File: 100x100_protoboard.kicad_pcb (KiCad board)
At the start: 2 copper layers, 97.8 x 96.5 mm, 422 parts, among them CON1 BARREL_JACK, CON2 USB_FEMALE_WITH_ID, CON3 USB_FEMALE_WITH_ID, J1 INTERCONNECT_1X03, J10 INTERCONNECT_1X03, J11 INTERCONNECT_1X03, J12 INTERCONNECT_1X03, J13 INTERCONNECT_1X03, J14 INTERCONNECT_1X03, J15 INTERCONNECT_1X03, J16 INTERCONNECT_1X03, J17 INTERCONNECT_1X03, J18 INTERCONNECT_1X03, J19 INTERCONNECT_1X03, J2 INTERCONNECT_1X03, J20 INTERCONNECT_1X03, J21 INTERCONNECT_1X03, J22 INTERCONNECT_1X03, J23 INTERCONNECT_1X03, J24 INTERCONNECT_1X03, J25 INTERCONNECT_1X03, J26 INTERCONNECT_1X03, J27 INTERCONNECT_1X03, J28 INTERCONNECT_1X03, J29 INTERCONNECT_1X03, J3 INTERCONNECT_1X03, J30 INTERCONNECT_1X03, J31 INTERCONNECT_1X03, J32 INTERCONNECT_1X03, J33 INTERCONNECT_1X03, J34 INTERCONNECT_1X03, J35 INTERCONNECT_1X03, J36 INTERCONNECT_1X03, J37 INTERCONNECT_1X03, J38 INTERCONNECT_1X03, J39 INTERCONNECT_1X03, J4 INTERCONNECT_1X03, J40 INTERCONNECT_1X03, J41 INTERCONNECT_1X03, J42 INTERCONNECT_1X03, J43 INTERCONNECT_1X03, J44 INTERCONNECT_1X03, J45 INTERCONNECT_1X03, J46 INTERCONNECT_1X03, J47 INTERCONNECT_1X03, J48 INTERCONNECT_1X03, J49 INTERCONNECT_1X03, J5 INTERCONNECT_1X03, J50 INTERCONNECT_1X03, J51 INTERCONNECT_1X03, J52 INTERCONNECT_1X03, J53 INTERCONNECT_1X03, J54 INTERCONNECT_1X03, J55 INTERCONNECT_1X03, J56 INTERCONNECT_1X03, J57 INTERCONNECT_1X03, J58 INTERCONNECT_1X03, J59 INTERCONNECT_1X03, J6 INTERCONNECT_1X03, J60 INTERCONNECT_1X03, J61 INTERCONNECT_1X03, J62 INTERCONNECT_1X03, J63 INTERCONNECT_1X03, J64 INTERCONNECT_1X03, J65 INTERCONNECT_1X02, J7 INTERCONNECT_1X03, J8 INTERCONNECT_1X03, J9 INTERCONNECT_1X03, P1 CONN_5, P1 CONN_6X2, P2 CONN_6X2, U1 LM7805CT

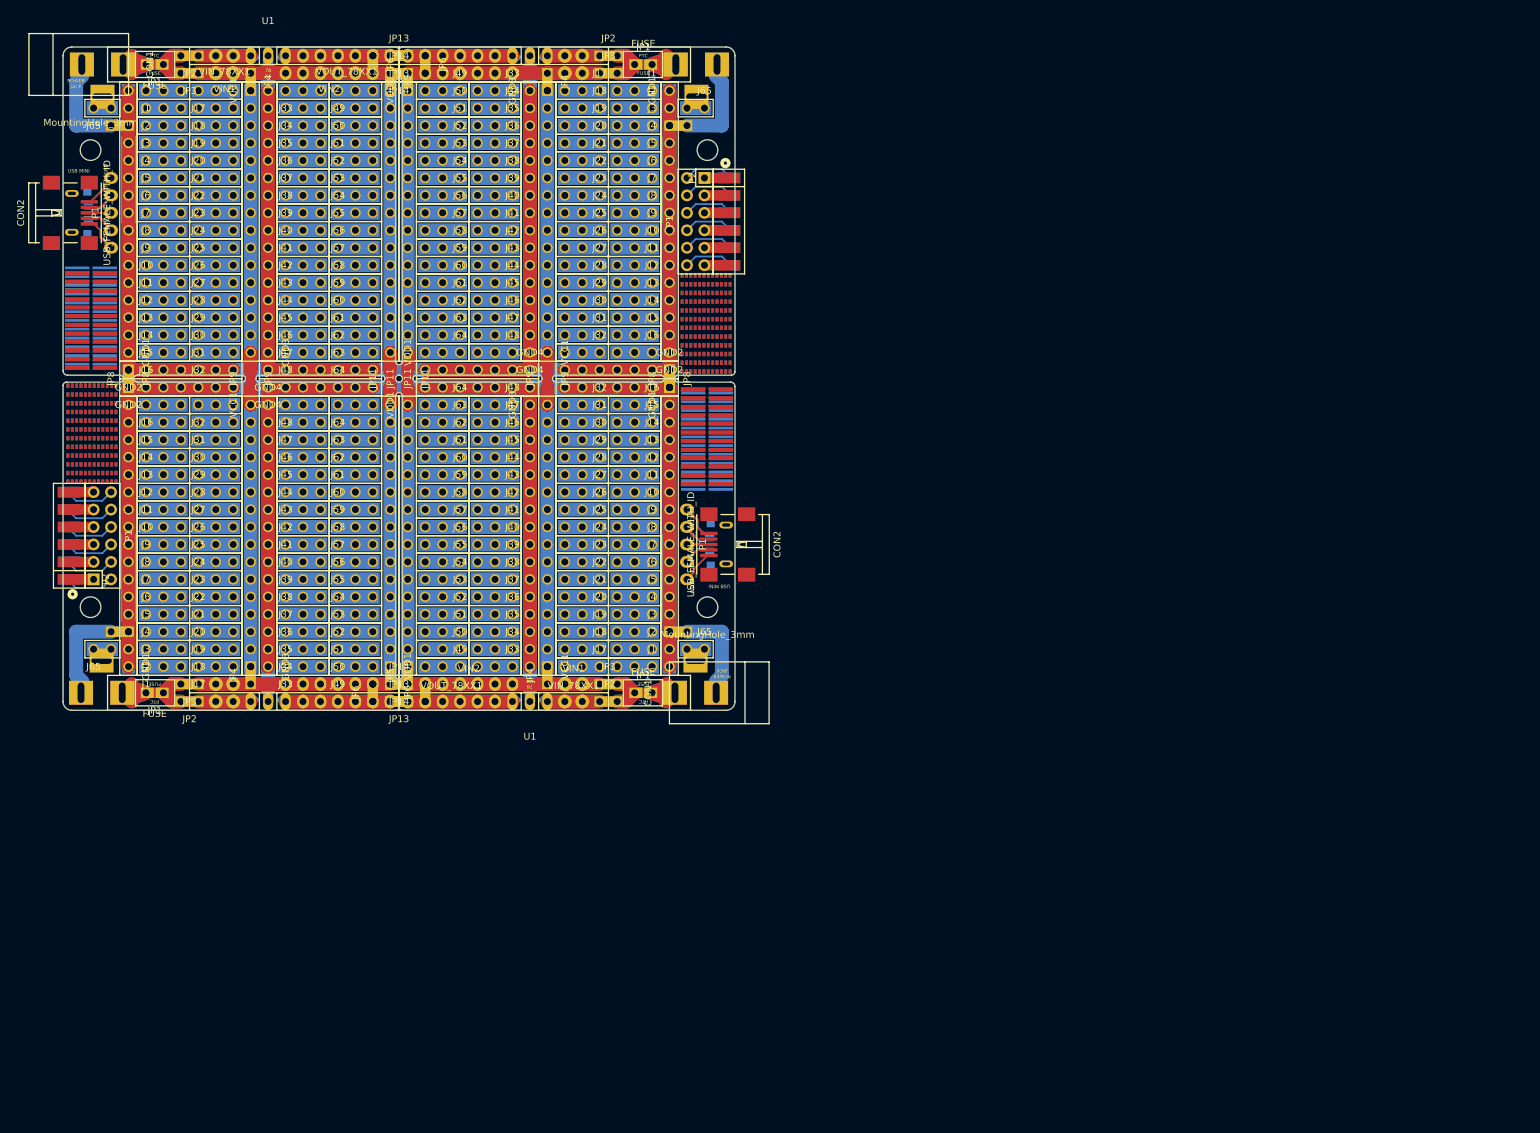
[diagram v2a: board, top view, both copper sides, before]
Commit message: increased pad size for SMD grid on bottom-left quarter
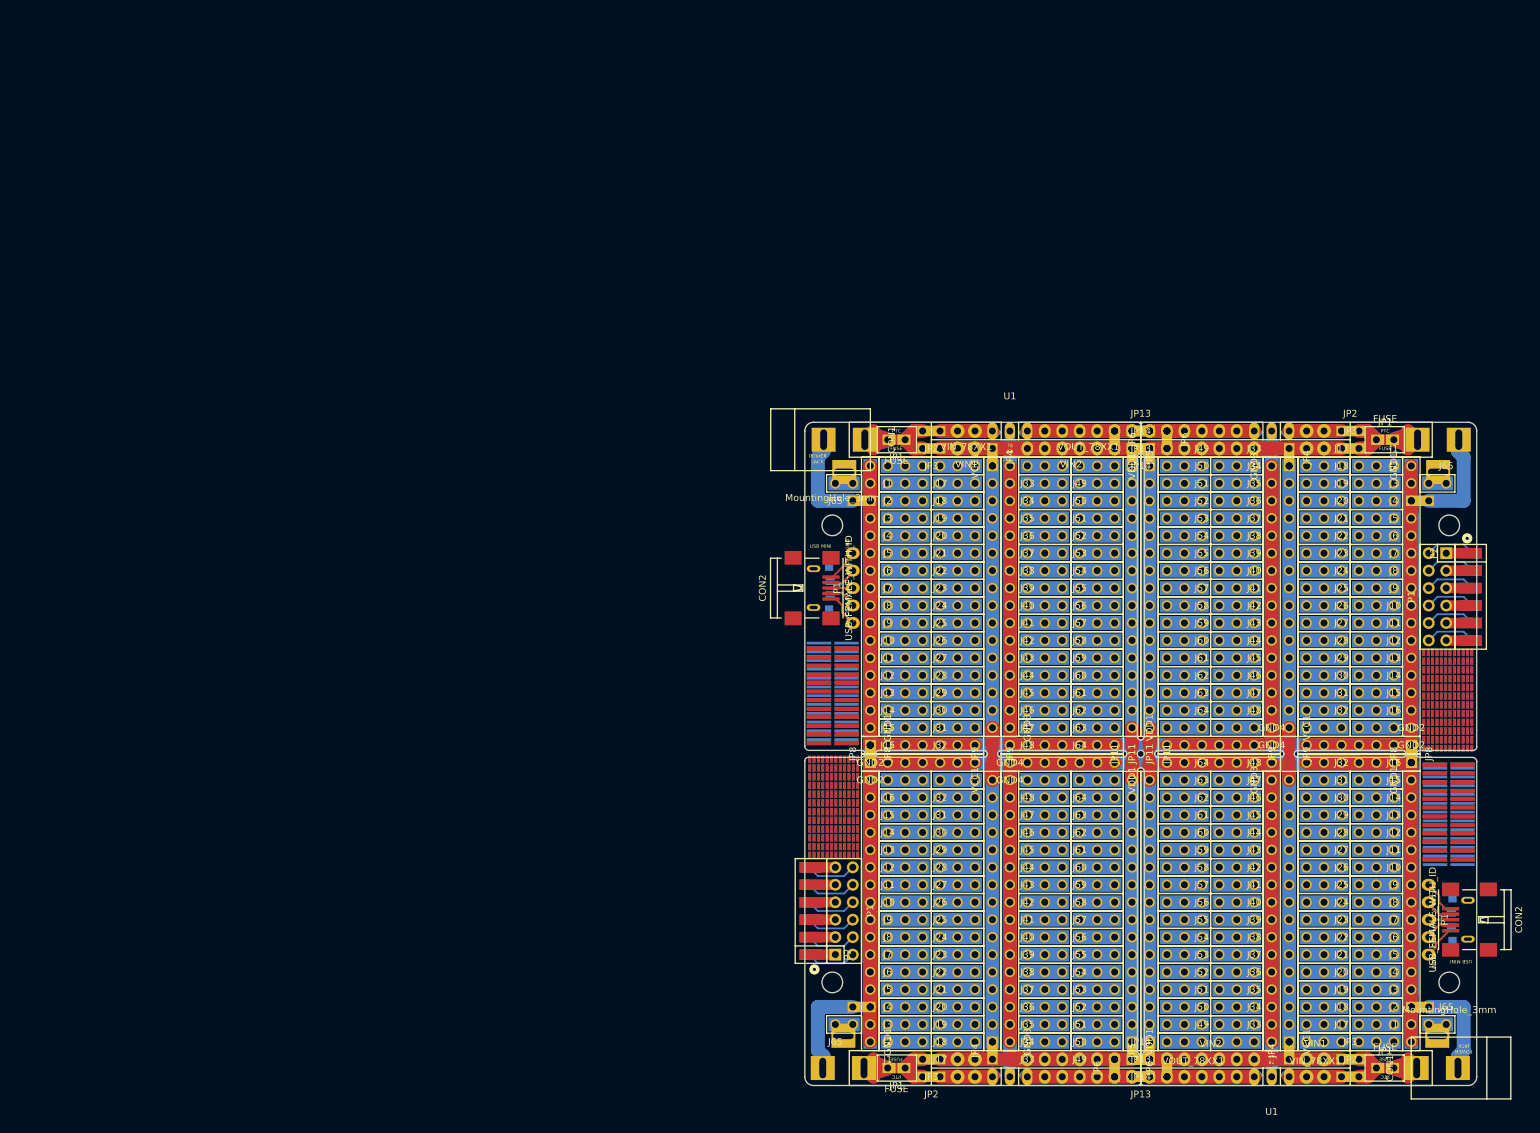
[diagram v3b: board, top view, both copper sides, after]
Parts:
- removed the C1 at (50.8, 117.1)
- removed the C1 at (91.4, 117.1)
- removed the C1 at (50.8, 25.1)
- removed the C1 at (91.4, 25.1)
- removed the C2 at (53.3, 117.1)
- removed the C2 at (88.9, 117.1)
- removed the C2 at (53.3, 25.1)
- removed the C2 at (88.9, 25.1)
- removed the CON1 at (24.6, 116.8)
- removed the CON1 at (117.5, 116.8)
- removed the CON1 at (24.8, 25.4)
- removed the CON1 at (117.6, 25.4)
- removed the CON2 at (116.2, 95.2)
- removed the CON2 at (26.0, 47.0)
- removed the CON3 at (116.3, 95.2)
- removed the CON3 at (25.9, 47.0)
- removed the F1 at (35.6, 116.8)
- removed the F1 at (106.7, 116.8)
- removed the F1 at (35.6, 25.4)
- removed the F1 at (106.7, 25.4)
- removed the F2 at (35.6, 116.8)
- removed the F2 at (106.7, 116.8)
- removed the F2 at (35.6, 25.4)
- removed the F2 at (106.7, 25.4)
- removed the GND1 at (31.8, 113.0)
- removed the GND1 at (110.5, 74.9)
- removed the GND1 at (31.8, 67.3)
- removed the GND1 at (110.5, 29.2)
- removed the GND2 at (31.8, 72.4)
- removed the GND2 at (110.5, 72.4)
- removed the GND2 at (31.8, 69.8)
- removed the GND2 at (110.5, 69.8)
- removed the GND3 at (52.1, 113.0)
- removed the GND3 at (90.2, 74.9)
- removed the GND3 at (52.1, 67.3)
- removed the GND3 at (90.2, 29.2)
- removed the GND4 at (52.1, 72.4)
- removed the GND4 at (90.2, 72.4)
- removed the GND4 at (52.1, 69.8)
- removed the GND4 at (90.2, 69.8)
- removed the J1 at (34.3, 113.0)
- removed the J1 at (108.0, 113.0)
- removed the J1 at (34.3, 29.2)
- removed the J1 at (108.0, 29.2)
- removed the J10 at (34.3, 90.2)
- removed the J10 at (108.0, 90.2)
- removed the J10 at (34.3, 52.1)
- removed the J10 at (108.0, 52.1)
- removed the J11 at (34.3, 87.6)
- removed the J11 at (108.0, 87.6)
- removed the J11 at (34.3, 54.6)
- removed the J11 at (108.0, 54.6)
- removed the J12 at (34.3, 85.1)
- removed the J12 at (108.0, 85.1)
- removed the J12 at (34.3, 57.1)
- removed the J12 at (108.0, 57.1)
- removed the J13 at (34.3, 82.5)
- removed the J13 at (108.0, 82.5)
- removed the J13 at (34.3, 59.7)
- removed the J13 at (108.0, 59.7)
- removed the J14 at (34.3, 80.0)
- removed the J14 at (108.0, 80.0)
- removed the J14 at (34.3, 62.2)
- removed the J14 at (108.0, 62.2)
- removed the J15 at (34.3, 77.5)
- removed the J15 at (108.0, 77.5)
- removed the J15 at (34.3, 64.8)
- removed the J15 at (108.0, 64.8)
- removed the J16 at (34.3, 74.9)
- removed the J16 at (108.0, 74.9)
- removed the J16 at (34.3, 67.3)
- removed the J16 at (108.0, 67.3)
- removed the J17 at (41.9, 113.0)
- removed the J17 at (100.3, 113.0)
- removed the J17 at (41.9, 29.2)
- removed the J17 at (100.3, 29.2)
- removed the J18 at (41.9, 110.5)
- removed the J18 at (100.3, 110.5)
- removed the J18 at (41.9, 31.8)
- removed the J18 at (100.3, 31.8)
- removed the J19 at (41.9, 108.0)
- removed the J19 at (100.3, 108.0)
- removed the J19 at (41.9, 34.3)
- removed the J19 at (100.3, 34.3)
- removed the J2 at (34.3, 110.5)
- removed the J2 at (108.0, 110.5)
- removed the J2 at (34.3, 31.8)
- removed the J2 at (108.0, 31.8)
- removed the J20 at (41.9, 105.4)
- removed the J20 at (100.3, 105.4)
- removed the J20 at (41.9, 36.8)
- removed the J20 at (100.3, 36.8)
- removed the J21 at (41.9, 102.9)
- removed the J21 at (100.3, 102.9)
- removed the J21 at (41.9, 39.4)
- removed the J21 at (100.3, 39.4)
- removed the J22 at (41.9, 100.3)
- removed the J22 at (100.3, 100.3)
- removed the J22 at (41.9, 41.9)
- removed the J22 at (100.3, 41.9)
- removed the J23 at (41.9, 97.8)
- removed the J23 at (100.3, 97.8)
- removed the J23 at (41.9, 44.5)
- removed the J23 at (100.3, 44.5)
- removed the J24 at (41.9, 95.2)
- removed the J24 at (100.3, 95.2)
- removed the J24 at (41.9, 47.0)
- removed the J24 at (100.3, 47.0)
- removed the J25 at (41.9, 92.7)
- removed the J25 at (100.3, 92.7)
- removed the J25 at (41.9, 49.5)
- removed the J25 at (100.3, 49.5)
- removed the J26 at (41.9, 90.2)
- removed the J26 at (100.3, 90.2)
- removed the J26 at (41.9, 52.1)
- removed the J26 at (100.3, 52.1)
- removed the J27 at (41.9, 87.6)
- removed the J27 at (100.3, 87.6)
- removed the J27 at (41.9, 54.6)
- removed the J27 at (100.3, 54.6)
- removed the J28 at (41.9, 85.1)
- removed the J28 at (100.3, 85.1)
- removed the J28 at (41.9, 57.1)
- removed the J28 at (100.3, 57.1)
- removed the J29 at (41.9, 82.5)
- removed the J29 at (100.3, 82.5)
- removed the J29 at (41.9, 59.7)
- removed the J29 at (100.3, 59.7)
- removed the J3 at (34.3, 108.0)
- removed the J3 at (108.0, 108.0)
- removed the J3 at (34.3, 34.3)
- removed the J3 at (108.0, 34.3)
- removed the J30 at (41.9, 80.0)
- removed the J30 at (100.3, 80.0)
- removed the J30 at (41.9, 62.2)
- removed the J30 at (100.3, 62.2)
- removed the J31 at (41.9, 77.5)
- removed the J31 at (100.3, 77.5)
- removed the J31 at (41.9, 64.8)
- removed the J31 at (100.3, 64.8)
- removed the J32 at (41.9, 74.9)
- removed the J32 at (100.3, 74.9)
- removed the J32 at (41.9, 67.3)
- removed the J32 at (100.3, 67.3)
- removed the J33 at (54.6, 113.0)
- removed the J33 at (87.6, 113.0)
- removed the J33 at (54.6, 29.2)
- removed the J33 at (87.6, 29.2)
- removed the J34 at (54.6, 110.5)
- removed the J34 at (87.6, 110.5)
- removed the J34 at (54.6, 31.8)
- removed the J34 at (87.6, 31.8)
- removed the J35 at (54.6, 108.0)
- removed the J35 at (87.6, 108.0)
- removed the J35 at (54.6, 34.3)
- removed the J35 at (87.6, 34.3)
- removed the J36 at (54.6, 105.4)
- removed the J36 at (87.6, 105.4)
- removed the J36 at (54.6, 36.8)
- removed the J36 at (87.6, 36.8)
- removed the J37 at (54.6, 102.9)
- removed the J37 at (87.6, 102.9)
- removed the J37 at (54.6, 39.4)
- removed the J37 at (87.6, 39.4)
- removed the J38 at (54.6, 100.3)
- removed the J38 at (87.6, 100.3)
- removed the J38 at (54.6, 41.9)
- removed the J38 at (87.6, 41.9)
- removed the J39 at (54.6, 97.8)
- removed the J39 at (87.6, 97.8)
- removed the J39 at (54.6, 44.5)
- removed the J39 at (87.6, 44.5)
- removed the J4 at (34.3, 105.4)
- removed the J4 at (108.0, 105.4)
- removed the J4 at (34.3, 36.8)
- removed the J4 at (108.0, 36.8)
- removed the J40 at (54.6, 95.2)
- removed the J40 at (87.6, 95.2)
- removed the J40 at (54.6, 47.0)
- removed the J40 at (87.6, 47.0)
- removed the J41 at (54.6, 92.7)
- removed the J41 at (87.6, 92.7)
- removed the J41 at (54.6, 49.5)
- removed the J41 at (87.6, 49.5)
- removed the J42 at (54.6, 90.2)
- removed the J42 at (87.6, 90.2)
- removed the J42 at (54.6, 52.1)
- removed the J42 at (87.6, 52.1)
- removed the J43 at (54.6, 87.6)
- removed the J43 at (87.6, 87.6)
- removed the J43 at (54.6, 54.6)
- removed the J43 at (87.6, 54.6)
- removed the J44 at (54.6, 85.1)
- removed the J44 at (87.6, 85.1)
- removed the J44 at (54.6, 57.1)
- removed the J44 at (87.6, 57.1)
- removed the J45 at (54.6, 82.5)
- removed the J45 at (87.6, 82.5)
- removed the J45 at (54.6, 59.7)
- removed the J45 at (87.6, 59.7)
- removed the J46 at (54.6, 80.0)
- removed the J46 at (87.6, 80.0)
- removed the J46 at (54.6, 62.2)
- removed the J46 at (87.6, 62.2)
- removed the J47 at (54.6, 77.5)
- removed the J47 at (87.6, 77.5)
- removed the J47 at (54.6, 64.8)
- removed the J47 at (87.6, 64.8)
- removed the J48 at (54.6, 74.9)
- removed the J48 at (87.6, 74.9)
- removed the J48 at (54.6, 67.3)
- removed the J48 at (87.6, 67.3)
- removed the J49 at (62.2, 113.0)
- removed the J49 at (80.0, 113.0)
- removed the J49 at (62.2, 29.2)
- removed the J49 at (80.0, 29.2)
- removed the J5 at (34.3, 102.9)
- removed the J5 at (108.0, 102.9)
- removed the J5 at (34.3, 39.4)
- removed the J5 at (108.0, 39.4)
- removed the J50 at (62.2, 110.5)
- removed the J50 at (80.0, 110.5)
- removed the J50 at (62.2, 31.8)
- removed the J50 at (80.0, 31.8)
- removed the J51 at (62.2, 108.0)
- removed the J51 at (80.0, 108.0)
- removed the J51 at (62.2, 34.3)
- removed the J51 at (80.0, 34.3)
- removed the J52 at (62.2, 105.4)
- removed the J52 at (80.0, 105.4)
- removed the J52 at (62.2, 36.8)
- removed the J52 at (80.0, 36.8)
- removed the J53 at (62.2, 102.9)
- removed the J53 at (80.0, 102.9)
- removed the J53 at (62.2, 39.4)
- removed the J53 at (80.0, 39.4)
- removed the J54 at (62.2, 100.3)
- removed the J54 at (80.0, 100.3)
- removed the J54 at (62.2, 41.9)
- removed the J54 at (80.0, 41.9)
- removed the J55 at (62.2, 97.8)
- removed the J55 at (80.0, 97.8)
- removed the J55 at (62.2, 44.5)
- removed the J55 at (80.0, 44.5)
- removed the J56 at (62.2, 95.2)
- removed the J56 at (80.0, 95.2)
- removed the J56 at (62.2, 47.0)
- removed the J56 at (80.0, 47.0)
- removed the J57 at (62.2, 92.7)
- removed the J57 at (80.0, 92.7)
- removed the J57 at (62.2, 49.5)
- removed the J57 at (80.0, 49.5)
- removed the J58 at (62.2, 90.2)
- removed the J58 at (80.0, 90.2)
- removed the J58 at (62.2, 52.1)
- removed the J58 at (80.0, 52.1)
- removed the J59 at (62.2, 87.6)
- removed the J59 at (80.0, 87.6)
- removed the J59 at (62.2, 54.6)
- removed the J59 at (80.0, 54.6)
- removed the J6 at (34.3, 100.3)
- removed the J6 at (108.0, 100.3)
- removed the J6 at (34.3, 41.9)
- removed the J6 at (108.0, 41.9)
- removed the J60 at (62.2, 85.1)
- removed the J60 at (80.0, 85.1)
- removed the J60 at (62.2, 57.1)
- removed the J60 at (80.0, 57.1)
- removed the J61 at (62.2, 82.5)
- removed the J61 at (80.0, 82.5)
- removed the J61 at (62.2, 59.7)
- removed the J61 at (80.0, 59.7)
- removed the J62 at (62.2, 80.0)
- removed the J62 at (80.0, 80.0)
- removed the J62 at (62.2, 62.2)
- removed the J62 at (80.0, 62.2)
- removed the J63 at (62.2, 77.5)
- removed the J63 at (80.0, 77.5)
- removed the J63 at (62.2, 64.8)
- removed the J63 at (80.0, 64.8)
- removed the J64 at (62.2, 74.9)
- removed the J64 at (80.0, 74.9)
- removed the J64 at (62.2, 67.3)
- removed the J64 at (80.0, 67.3)
- removed the J65 at (26.7, 110.5)
- removed the J65 at (115.6, 110.5)
- removed the J65 at (26.7, 31.8)
- removed the J65 at (115.6, 31.8)
- removed the J7 at (34.3, 97.8)
- removed the J7 at (108.0, 97.8)
- removed the J7 at (34.3, 44.5)
- removed the J7 at (108.0, 44.5)
- removed the J8 at (34.3, 95.2)
- removed the J8 at (108.0, 95.2)
- removed the J8 at (34.3, 47.0)
- removed the J8 at (108.0, 47.0)
- removed the J9 at (34.3, 92.7)
- removed the J9 at (108.0, 92.7)
- removed the J9 at (34.3, 49.5)
- removed the J9 at (108.0, 49.5)
- removed the JP1 at (35.6, 116.8)
- removed the JP1 at (106.7, 116.8)
- removed the JP1 at (35.6, 25.4)
- removed the JP1 at (106.7, 25.4)
- removed the JP10 at (69.8, 71.1) (x2)
- removed the JP10 at (72.4, 71.1) (x2)
- removed the JP11 at (69.8, 71.1) (x2)
- removed the JP11 at (72.4, 71.1) (x2)
- removed the JP12 at (71.1, 72.4) (x2)
- removed the JP12 at (71.1, 69.8) (x2)
- removed the JP13 at (71.1, 118.1) (x2)
- removed the JP13 at (71.1, 24.1) (x2)
- removed the JP14 at (71.1, 115.6) (x2)
- removed the JP14 at (71.1, 26.7) (x2)
- removed the JP15 at (49.5, 71.1) (x2)
- removed the JP15 at (92.7, 71.1) (x2)
- removed the JP2 at (40.6, 118.1)
- removed the JP2 at (101.6, 118.1)
- removed the JP2 at (40.6, 24.1)
- removed the JP2 at (101.6, 24.1)
- removed the JP3 at (40.6, 115.6)
- removed the JP3 at (101.6, 115.6)
- removed the JP3 at (40.6, 26.7)
- removed the JP3 at (101.6, 26.7)
- removed the JP4 at (49.5, 114.3)
- removed the JP4 at (92.7, 114.3)
- removed the JP4 at (49.5, 27.9)
- removed the JP4 at (92.7, 27.9)
- removed the JP5 at (69.8, 114.3)
- removed the JP5 at (72.4, 114.3)
- removed the JP5 at (69.8, 27.9)
- removed the JP5 at (72.4, 27.9)
- removed the JP6 at (67.3, 116.8)
- removed the JP6 at (74.9, 116.8)
- removed the JP6 at (67.3, 25.4)
- removed the JP6 at (74.9, 25.4)
- removed the JP7 at (30.5, 108.0)
- removed the JP7 at (111.8, 108.0)
- removed the JP7 at (30.5, 34.3)
- removed the JP7 at (111.8, 34.3)
- removed the JP8 at (31.8, 71.1) (x2)
- removed the JP8 at (110.5, 71.1) (x2)
- removed the JP9 at (49.5, 71.1) (x2)
- removed the JP9 at (92.7, 71.1) (x2)
- removed the MountingHole_3mm at (26.2, 104.4)
- removed the MountingHole_3mm at (116.0, 104.4)
- removed the MountingHole_3mm at (26.2, 37.9)
- removed the MountingHole_3mm at (116.0, 37.9)
- removed the P1 at (27.9, 94.0)
- removed the P1 at (113.0, 95.2)
- removed the P1 at (29.2, 47.0)
- removed the P1 at (114.3, 48.3)
- removed the P2 at (23.1, 100.3)
- removed the P2 at (119.1, 41.9)
- removed the Ref** at (25.8, 84.2) (x2)
- removed the Ref** at (116.0, 74.8)
- removed the Ref** at (116.0, 79.9)
- removed the Ref** at (116.0, 85.0)
- removed the Ref** at (26.3, 57.2)
- removed the Ref** at (26.3, 62.3)
- removed the Ref** at (26.3, 67.4)
- removed the Ref** at (26.3, 67.6)
- removed the Ref** at (26.3, 62.7)
- removed the Ref** at (26.3, 57.7)
- removed the Ref** at (116.5, 68.2) (x2)
- removed the Ref** at (25.8, 79.1) (x2)
- removed the Ref** at (116.5, 63.1) (x2)
- removed the Ref** at (116.5, 58.0) (x2)
- removed the Ref** at (25.8, 74.1) (x2)
- removed the Ref** at (115.9, 84.5)
- removed the Ref** at (115.9, 79.6)
- removed the Ref** at (115.9, 74.6)
- removed the U1 at (52.1, 118.1)
- removed the U1 at (90.2, 118.1)
- removed the U1 at (52.1, 24.1)
- removed the U1 at (90.2, 24.1)
- removed the VCC1 at (49.5, 74.9)
- removed the VCC1 at (92.7, 113.0)
- removed the VCC1 at (49.5, 29.2)
- removed the VCC1 at (92.7, 67.3)
- removed the VDD1 at (69.8, 113.0)
- removed the VDD1 at (72.4, 74.9)
- removed the VDD1 at (69.8, 67.3)
- removed the VDD1 at (72.4, 29.2)
- removed the VIN1 at (45.7, 115.6)
- removed the VIN1 at (96.5, 115.6)
- removed the VIN1 at (45.7, 26.7)
- removed the VIN1 at (96.5, 26.7)
- removed the VIN2 at (61.0, 115.6)
- removed the VIN2 at (81.3, 115.6)
- removed the VIN2 at (61.0, 26.7)
- removed the VIN2 at (81.3, 26.7)
- removed the VIN_78XX1 at (45.7, 118.1)
- removed the VIN_78XX1 at (96.5, 118.1)
- removed the VIN_78XX1 at (45.7, 24.1)
- removed the VIN_78XX1 at (96.5, 24.1)
- removed the VOUT_78XX1 at (63.5, 118.1)
- removed the VOUT_78XX1 at (78.7, 118.1)
- removed the VOUT_78XX1 at (63.5, 24.1)
- removed the VOUT_78XX1 at (78.7, 24.1)
- added C1: u33, Capacitors_SMD:C_0805_HandSoldering, B.Cu at (199.4, 79.8)
- added C1: u33, Capacitors_SMD:C_0805_HandSoldering, B.Cu at (199.4, 171.7)
- added C1: u33, Capacitors_SMD:C_0805_HandSoldering, B.Cu at (158.8, 79.8)
- added C1: u33, Capacitors_SMD:C_0805_HandSoldering, B.Cu at (158.8, 171.7)
- added C2: u1, Capacitors_SMD:C_0805_HandSoldering, B.Cu at (196.8, 79.8)
- added C2: u1, Capacitors_SMD:C_0805_HandSoldering, B.Cu at (196.8, 171.7)
- added C2: u1, Capacitors_SMD:C_0805_HandSoldering, B.Cu at (161.3, 79.8)
- added C2: u1, Capacitors_SMD:C_0805_HandSoldering, B.Cu at (161.3, 171.7)
- added CON1: BARREL_JACK, Connect:BARREL_JACK, B.Cu at (225.6, 80.0)
- added CON1: BARREL_JACK, Connect:BARREL_JACK, F.Cu at (225.4, 171.4)
- added CON1: BARREL_JACK, Connect:BARREL_JACK, F.Cu at (132.7, 80.0)
- added CON1: BARREL_JACK, Connect:BARREL_JACK, B.Cu at (132.6, 171.4)
- added CON2: USB_FEMALE_WITH_ID, Connectors:USB_Mini-B_Female, F.Cu at (224.2, 149.9)
- added CON2: USB_FEMALE_WITH_ID, Connectors:USB_Mini-B_Female, F.Cu at (134.0, 101.6)
- added CON3: USB_FEMALE_WITH_ID, Connectors:USB_Micro-B_Female_Wellco_AUSB_1011_05S2, B.Cu at (224.3, 149.9)
- added CON3: USB_FEMALE_WITH_ID, Connectors:USB_Micro-B_Female_Wellco_AUSB_1011_05S2, B.Cu at (133.9, 101.6)
- added F1: FUSE, Muonde:CC12ZZ, B.Cu at (214.6, 80.0)
- added F1: FUSE, Muonde:CC12ZZ, F.Cu at (214.6, 171.4)
- added F1: FUSE, Muonde:CC12ZZ, F.Cu at (143.5, 80.0)
- added F1: FUSE, Muonde:CC12ZZ, B.Cu at (143.5, 171.4)
- added F2: FUSE, Muonde:CC12ZZ, F.Cu at (214.6, 80.0)
- added F2: FUSE, Muonde:CC12ZZ, B.Cu at (214.6, 171.4)
- added F2: FUSE, Muonde:CC12ZZ, B.Cu at (143.5, 80.0)
- added F2: FUSE, Muonde:CC12ZZ, F.Cu at (143.5, 171.4)
- added GND1: INTERCONNECT_1X16, 2.54mm_Pin_Headers:Interconnect_1x16, F.Cu at (218.4, 83.8)
- added GND1: INTERCONNECT_1X16, 2.54mm_Pin_Headers:Interconnect_1x16, F.Cu at (218.4, 129.5)
- added GND1: INTERCONNECT_1X16, 2.54mm_Pin_Headers:Interconnect_1x16, F.Cu at (139.7, 121.9)
- added GND1: INTERCONNECT_1X16, 2.54mm_Pin_Headers:Interconnect_1x16, F.Cu at (139.7, 167.6)
- added GND2: INTERCONNECT_1X07, 2.54mm_Pin_Headers:Interconnect_1x07, F.Cu at (218.4, 124.5)
- added GND2: INTERCONNECT_1X07, 2.54mm_Pin_Headers:Interconnect_1x07, F.Cu at (218.4, 127.0)
- added GND2: INTERCONNECT_1X07, 2.54mm_Pin_Headers:Interconnect_1x07, F.Cu at (139.7, 124.5)
- added GND2: INTERCONNECT_1X07, 2.54mm_Pin_Headers:Interconnect_1x07, F.Cu at (139.7, 127.0)
- added GND3: INTERCONNECT_1X16, 2.54mm_Pin_Headers:Interconnect_1x16, F.Cu at (198.1, 83.8)
- added GND3: INTERCONNECT_1X16, 2.54mm_Pin_Headers:Interconnect_1x16, F.Cu at (198.1, 129.5)
- added GND3: INTERCONNECT_1X16, 2.54mm_Pin_Headers:Interconnect_1x16, F.Cu at (160.0, 121.9)
- added GND3: INTERCONNECT_1X16, 2.54mm_Pin_Headers:Interconnect_1x16, F.Cu at (160.0, 167.6)
- added GND4: INTERCONNECT_1X07, 2.54mm_Pin_Headers:Interconnect_1x07, F.Cu at (198.1, 124.5)
- added GND4: INTERCONNECT_1X07, 2.54mm_Pin_Headers:Interconnect_1x07, F.Cu at (198.1, 127.0)
- added GND4: INTERCONNECT_1X07, 2.54mm_Pin_Headers:Interconnect_1x07, F.Cu at (160.0, 124.5)
- added GND4: INTERCONNECT_1X07, 2.54mm_Pin_Headers:Interconnect_1x07, F.Cu at (160.0, 127.0)
- added J1: INTERCONNECT_1X03, 2.54mm_Pin_Headers:Interconnect_1x03, F.Cu at (215.9, 83.8)
- added J1: INTERCONNECT_1X03, 2.54mm_Pin_Headers:Interconnect_1x03, F.Cu at (215.9, 167.6)
- added J1: INTERCONNECT_1X03, 2.54mm_Pin_Headers:Interconnect_1x03, F.Cu at (142.2, 83.8)
- added J1: INTERCONNECT_1X03, 2.54mm_Pin_Headers:Interconnect_1x03, F.Cu at (142.2, 167.6)
- added J10: INTERCONNECT_1X03, 2.54mm_Pin_Headers:Interconnect_1x03, F.Cu at (215.9, 106.7)
- added J10: INTERCONNECT_1X03, 2.54mm_Pin_Headers:Interconnect_1x03, F.Cu at (215.9, 144.8)
- added J10: INTERCONNECT_1X03, 2.54mm_Pin_Headers:Interconnect_1x03, F.Cu at (142.2, 106.7)
- added J10: INTERCONNECT_1X03, 2.54mm_Pin_Headers:Interconnect_1x03, F.Cu at (142.2, 144.8)
- added J11: INTERCONNECT_1X03, 2.54mm_Pin_Headers:Interconnect_1x03, F.Cu at (215.9, 109.2)
- added J11: INTERCONNECT_1X03, 2.54mm_Pin_Headers:Interconnect_1x03, F.Cu at (215.9, 142.2)
- added J11: INTERCONNECT_1X03, 2.54mm_Pin_Headers:Interconnect_1x03, F.Cu at (142.2, 109.2)
- added J11: INTERCONNECT_1X03, 2.54mm_Pin_Headers:Interconnect_1x03, F.Cu at (142.2, 142.2)
- added J12: INTERCONNECT_1X03, 2.54mm_Pin_Headers:Interconnect_1x03, F.Cu at (215.9, 111.8)
- added J12: INTERCONNECT_1X03, 2.54mm_Pin_Headers:Interconnect_1x03, F.Cu at (215.9, 139.7)
- added J12: INTERCONNECT_1X03, 2.54mm_Pin_Headers:Interconnect_1x03, F.Cu at (142.2, 111.8)
- added J12: INTERCONNECT_1X03, 2.54mm_Pin_Headers:Interconnect_1x03, F.Cu at (142.2, 139.7)
- added J13: INTERCONNECT_1X03, 2.54mm_Pin_Headers:Interconnect_1x03, F.Cu at (215.9, 114.3)
- added J13: INTERCONNECT_1X03, 2.54mm_Pin_Headers:Interconnect_1x03, F.Cu at (215.9, 137.2)
- added J13: INTERCONNECT_1X03, 2.54mm_Pin_Headers:Interconnect_1x03, F.Cu at (142.2, 114.3)
- added J13: INTERCONNECT_1X03, 2.54mm_Pin_Headers:Interconnect_1x03, F.Cu at (142.2, 137.2)
- added J14: INTERCONNECT_1X03, 2.54mm_Pin_Headers:Interconnect_1x03, F.Cu at (215.9, 116.8)
- added J14: INTERCONNECT_1X03, 2.54mm_Pin_Headers:Interconnect_1x03, F.Cu at (215.9, 134.6)
- added J14: INTERCONNECT_1X03, 2.54mm_Pin_Headers:Interconnect_1x03, F.Cu at (142.2, 116.8)
- added J14: INTERCONNECT_1X03, 2.54mm_Pin_Headers:Interconnect_1x03, F.Cu at (142.2, 134.6)
- added J15: INTERCONNECT_1X03, 2.54mm_Pin_Headers:Interconnect_1x03, F.Cu at (215.9, 119.4)
- added J15: INTERCONNECT_1X03, 2.54mm_Pin_Headers:Interconnect_1x03, F.Cu at (215.9, 132.1)
- added J15: INTERCONNECT_1X03, 2.54mm_Pin_Headers:Interconnect_1x03, F.Cu at (142.2, 119.4)
- added J15: INTERCONNECT_1X03, 2.54mm_Pin_Headers:Interconnect_1x03, F.Cu at (142.2, 132.1)
- added J16: INTERCONNECT_1X03, 2.54mm_Pin_Headers:Interconnect_1x03, F.Cu at (215.9, 121.9)
- added J16: INTERCONNECT_1X03, 2.54mm_Pin_Headers:Interconnect_1x03, F.Cu at (215.9, 129.5)
- added J16: INTERCONNECT_1X03, 2.54mm_Pin_Headers:Interconnect_1x03, F.Cu at (142.2, 121.9)
- added J16: INTERCONNECT_1X03, 2.54mm_Pin_Headers:Interconnect_1x03, F.Cu at (142.2, 129.5)
- added J17: INTERCONNECT_1X03, 2.54mm_Pin_Headers:Interconnect_1x03, F.Cu at (208.3, 83.8)
- added J17: INTERCONNECT_1X03, 2.54mm_Pin_Headers:Interconnect_1x03, F.Cu at (208.3, 167.6)
- added J17: INTERCONNECT_1X03, 2.54mm_Pin_Headers:Interconnect_1x03, F.Cu at (149.9, 83.8)
- added J17: INTERCONNECT_1X03, 2.54mm_Pin_Headers:Interconnect_1x03, F.Cu at (149.9, 167.6)
- added J18: INTERCONNECT_1X03, 2.54mm_Pin_Headers:Interconnect_1x03, F.Cu at (208.3, 86.4)
- added J18: INTERCONNECT_1X03, 2.54mm_Pin_Headers:Interconnect_1x03, F.Cu at (208.3, 165.1)
- added J18: INTERCONNECT_1X03, 2.54mm_Pin_Headers:Interconnect_1x03, F.Cu at (149.9, 86.4)
- added J18: INTERCONNECT_1X03, 2.54mm_Pin_Headers:Interconnect_1x03, F.Cu at (149.9, 165.1)
- added J19: INTERCONNECT_1X03, 2.54mm_Pin_Headers:Interconnect_1x03, F.Cu at (208.3, 88.9)
- added J19: INTERCONNECT_1X03, 2.54mm_Pin_Headers:Interconnect_1x03, F.Cu at (208.3, 162.6)
- added J19: INTERCONNECT_1X03, 2.54mm_Pin_Headers:Interconnect_1x03, F.Cu at (149.9, 88.9)
- added J19: INTERCONNECT_1X03, 2.54mm_Pin_Headers:Interconnect_1x03, F.Cu at (149.9, 162.6)
- added J2: INTERCONNECT_1X03, 2.54mm_Pin_Headers:Interconnect_1x03, F.Cu at (215.9, 86.4)
- added J2: INTERCONNECT_1X03, 2.54mm_Pin_Headers:Interconnect_1x03, F.Cu at (215.9, 165.1)
- added J2: INTERCONNECT_1X03, 2.54mm_Pin_Headers:Interconnect_1x03, F.Cu at (142.2, 86.4)
- added J2: INTERCONNECT_1X03, 2.54mm_Pin_Headers:Interconnect_1x03, F.Cu at (142.2, 165.1)
- added J20: INTERCONNECT_1X03, 2.54mm_Pin_Headers:Interconnect_1x03, F.Cu at (208.3, 91.4)
- added J20: INTERCONNECT_1X03, 2.54mm_Pin_Headers:Interconnect_1x03, F.Cu at (208.3, 160.0)
- added J20: INTERCONNECT_1X03, 2.54mm_Pin_Headers:Interconnect_1x03, F.Cu at (149.9, 91.4)
- added J20: INTERCONNECT_1X03, 2.54mm_Pin_Headers:Interconnect_1x03, F.Cu at (149.9, 160.0)
- added J21: INTERCONNECT_1X03, 2.54mm_Pin_Headers:Interconnect_1x03, F.Cu at (208.3, 94.0)
- added J21: INTERCONNECT_1X03, 2.54mm_Pin_Headers:Interconnect_1x03, F.Cu at (208.3, 157.5)
- added J21: INTERCONNECT_1X03, 2.54mm_Pin_Headers:Interconnect_1x03, F.Cu at (149.9, 94.0)
- added J21: INTERCONNECT_1X03, 2.54mm_Pin_Headers:Interconnect_1x03, F.Cu at (149.9, 157.5)
- added J22: INTERCONNECT_1X03, 2.54mm_Pin_Headers:Interconnect_1x03, F.Cu at (208.3, 96.5)
- added J22: INTERCONNECT_1X03, 2.54mm_Pin_Headers:Interconnect_1x03, F.Cu at (208.3, 154.9)
- added J22: INTERCONNECT_1X03, 2.54mm_Pin_Headers:Interconnect_1x03, F.Cu at (149.9, 96.5)
- added J22: INTERCONNECT_1X03, 2.54mm_Pin_Headers:Interconnect_1x03, F.Cu at (149.9, 154.9)
- added J23: INTERCONNECT_1X03, 2.54mm_Pin_Headers:Interconnect_1x03, F.Cu at (208.3, 99.1)
- added J23: INTERCONNECT_1X03, 2.54mm_Pin_Headers:Interconnect_1x03, F.Cu at (208.3, 152.4)
- added J23: INTERCONNECT_1X03, 2.54mm_Pin_Headers:Interconnect_1x03, F.Cu at (149.9, 99.1)
- added J23: INTERCONNECT_1X03, 2.54mm_Pin_Headers:Interconnect_1x03, F.Cu at (149.9, 152.4)
- added J24: INTERCONNECT_1X03, 2.54mm_Pin_Headers:Interconnect_1x03, F.Cu at (208.3, 101.6)
- added J24: INTERCONNECT_1X03, 2.54mm_Pin_Headers:Interconnect_1x03, F.Cu at (208.3, 149.9)
- added J24: INTERCONNECT_1X03, 2.54mm_Pin_Headers:Interconnect_1x03, F.Cu at (149.9, 101.6)
- added J24: INTERCONNECT_1X03, 2.54mm_Pin_Headers:Interconnect_1x03, F.Cu at (149.9, 149.9)
- added J25: INTERCONNECT_1X03, 2.54mm_Pin_Headers:Interconnect_1x03, F.Cu at (208.3, 104.1)
- added J25: INTERCONNECT_1X03, 2.54mm_Pin_Headers:Interconnect_1x03, F.Cu at (208.3, 147.3)
- added J25: INTERCONNECT_1X03, 2.54mm_Pin_Headers:Interconnect_1x03, F.Cu at (149.9, 104.1)
- added J25: INTERCONNECT_1X03, 2.54mm_Pin_Headers:Interconnect_1x03, F.Cu at (149.9, 147.3)
- added J26: INTERCONNECT_1X03, 2.54mm_Pin_Headers:Interconnect_1x03, F.Cu at (208.3, 106.7)
- added J26: INTERCONNECT_1X03, 2.54mm_Pin_Headers:Interconnect_1x03, F.Cu at (208.3, 144.8)
- added J26: INTERCONNECT_1X03, 2.54mm_Pin_Headers:Interconnect_1x03, F.Cu at (149.9, 106.7)
- added J26: INTERCONNECT_1X03, 2.54mm_Pin_Headers:Interconnect_1x03, F.Cu at (149.9, 144.8)
- added J27: INTERCONNECT_1X03, 2.54mm_Pin_Headers:Interconnect_1x03, F.Cu at (208.3, 109.2)
- added J27: INTERCONNECT_1X03, 2.54mm_Pin_Headers:Interconnect_1x03, F.Cu at (208.3, 142.2)
- added J27: INTERCONNECT_1X03, 2.54mm_Pin_Headers:Interconnect_1x03, F.Cu at (149.9, 109.2)
- added J27: INTERCONNECT_1X03, 2.54mm_Pin_Headers:Interconnect_1x03, F.Cu at (149.9, 142.2)
- added J28: INTERCONNECT_1X03, 2.54mm_Pin_Headers:Interconnect_1x03, F.Cu at (208.3, 111.8)
- added J28: INTERCONNECT_1X03, 2.54mm_Pin_Headers:Interconnect_1x03, F.Cu at (208.3, 139.7)
- added J28: INTERCONNECT_1X03, 2.54mm_Pin_Headers:Interconnect_1x03, F.Cu at (149.9, 111.8)
- added J28: INTERCONNECT_1X03, 2.54mm_Pin_Headers:Interconnect_1x03, F.Cu at (149.9, 139.7)
- added J29: INTERCONNECT_1X03, 2.54mm_Pin_Headers:Interconnect_1x03, F.Cu at (208.3, 114.3)
- added J29: INTERCONNECT_1X03, 2.54mm_Pin_Headers:Interconnect_1x03, F.Cu at (208.3, 137.2)
- added J29: INTERCONNECT_1X03, 2.54mm_Pin_Headers:Interconnect_1x03, F.Cu at (149.9, 114.3)
- added J29: INTERCONNECT_1X03, 2.54mm_Pin_Headers:Interconnect_1x03, F.Cu at (149.9, 137.2)
- added J3: INTERCONNECT_1X03, 2.54mm_Pin_Headers:Interconnect_1x03, F.Cu at (215.9, 88.9)
- added J3: INTERCONNECT_1X03, 2.54mm_Pin_Headers:Interconnect_1x03, F.Cu at (215.9, 162.6)
- added J3: INTERCONNECT_1X03, 2.54mm_Pin_Headers:Interconnect_1x03, F.Cu at (142.2, 88.9)
- added J3: INTERCONNECT_1X03, 2.54mm_Pin_Headers:Interconnect_1x03, F.Cu at (142.2, 162.6)
- added J30: INTERCONNECT_1X03, 2.54mm_Pin_Headers:Interconnect_1x03, F.Cu at (208.3, 116.8)
- added J30: INTERCONNECT_1X03, 2.54mm_Pin_Headers:Interconnect_1x03, F.Cu at (208.3, 134.6)
- added J30: INTERCONNECT_1X03, 2.54mm_Pin_Headers:Interconnect_1x03, F.Cu at (149.9, 116.8)
- added J30: INTERCONNECT_1X03, 2.54mm_Pin_Headers:Interconnect_1x03, F.Cu at (149.9, 134.6)
- added J31: INTERCONNECT_1X03, 2.54mm_Pin_Headers:Interconnect_1x03, F.Cu at (208.3, 119.4)
- added J31: INTERCONNECT_1X03, 2.54mm_Pin_Headers:Interconnect_1x03, F.Cu at (208.3, 132.1)
- added J31: INTERCONNECT_1X03, 2.54mm_Pin_Headers:Interconnect_1x03, F.Cu at (149.9, 119.4)
- added J31: INTERCONNECT_1X03, 2.54mm_Pin_Headers:Interconnect_1x03, F.Cu at (149.9, 132.1)
- added J32: INTERCONNECT_1X03, 2.54mm_Pin_Headers:Interconnect_1x03, F.Cu at (208.3, 121.9)
- added J32: INTERCONNECT_1X03, 2.54mm_Pin_Headers:Interconnect_1x03, F.Cu at (208.3, 129.5)
- added J32: INTERCONNECT_1X03, 2.54mm_Pin_Headers:Interconnect_1x03, F.Cu at (149.9, 121.9)
- added J32: INTERCONNECT_1X03, 2.54mm_Pin_Headers:Interconnect_1x03, F.Cu at (149.9, 129.5)
- added J33: INTERCONNECT_1X03, 2.54mm_Pin_Headers:Interconnect_1x03, F.Cu at (195.6, 83.8)
- added J33: INTERCONNECT_1X03, 2.54mm_Pin_Headers:Interconnect_1x03, F.Cu at (195.6, 167.6)
- added J33: INTERCONNECT_1X03, 2.54mm_Pin_Headers:Interconnect_1x03, F.Cu at (162.6, 83.8)
- added J33: INTERCONNECT_1X03, 2.54mm_Pin_Headers:Interconnect_1x03, F.Cu at (162.6, 167.6)
- added J34: INTERCONNECT_1X03, 2.54mm_Pin_Headers:Interconnect_1x03, F.Cu at (195.6, 86.4)
- added J34: INTERCONNECT_1X03, 2.54mm_Pin_Headers:Interconnect_1x03, F.Cu at (195.6, 165.1)
- added J34: INTERCONNECT_1X03, 2.54mm_Pin_Headers:Interconnect_1x03, F.Cu at (162.6, 86.4)
- added J34: INTERCONNECT_1X03, 2.54mm_Pin_Headers:Interconnect_1x03, F.Cu at (162.6, 165.1)
- added J35: INTERCONNECT_1X03, 2.54mm_Pin_Headers:Interconnect_1x03, F.Cu at (195.6, 88.9)
- added J35: INTERCONNECT_1X03, 2.54mm_Pin_Headers:Interconnect_1x03, F.Cu at (195.6, 162.6)
- added J35: INTERCONNECT_1X03, 2.54mm_Pin_Headers:Interconnect_1x03, F.Cu at (162.6, 88.9)
- added J35: INTERCONNECT_1X03, 2.54mm_Pin_Headers:Interconnect_1x03, F.Cu at (162.6, 162.6)
- added J36: INTERCONNECT_1X03, 2.54mm_Pin_Headers:Interconnect_1x03, F.Cu at (195.6, 91.4)
- added J36: INTERCONNECT_1X03, 2.54mm_Pin_Headers:Interconnect_1x03, F.Cu at (195.6, 160.0)
- added J36: INTERCONNECT_1X03, 2.54mm_Pin_Headers:Interconnect_1x03, F.Cu at (162.6, 91.4)
- added J36: INTERCONNECT_1X03, 2.54mm_Pin_Headers:Interconnect_1x03, F.Cu at (162.6, 160.0)
- added J37: INTERCONNECT_1X03, 2.54mm_Pin_Headers:Interconnect_1x03, F.Cu at (195.6, 94.0)
- added J37: INTERCONNECT_1X03, 2.54mm_Pin_Headers:Interconnect_1x03, F.Cu at (195.6, 157.5)
- added J37: INTERCONNECT_1X03, 2.54mm_Pin_Headers:Interconnect_1x03, F.Cu at (162.6, 94.0)
- added J37: INTERCONNECT_1X03, 2.54mm_Pin_Headers:Interconnect_1x03, F.Cu at (162.6, 157.5)
- added J38: INTERCONNECT_1X03, 2.54mm_Pin_Headers:Interconnect_1x03, F.Cu at (195.6, 96.5)
- added J38: INTERCONNECT_1X03, 2.54mm_Pin_Headers:Interconnect_1x03, F.Cu at (195.6, 154.9)
- added J38: INTERCONNECT_1X03, 2.54mm_Pin_Headers:Interconnect_1x03, F.Cu at (162.6, 96.5)
- added J38: INTERCONNECT_1X03, 2.54mm_Pin_Headers:Interconnect_1x03, F.Cu at (162.6, 154.9)
- added J39: INTERCONNECT_1X03, 2.54mm_Pin_Headers:Interconnect_1x03, F.Cu at (195.6, 99.1)
- added J39: INTERCONNECT_1X03, 2.54mm_Pin_Headers:Interconnect_1x03, F.Cu at (195.6, 152.4)
- added J39: INTERCONNECT_1X03, 2.54mm_Pin_Headers:Interconnect_1x03, F.Cu at (162.6, 99.1)
- added J39: INTERCONNECT_1X03, 2.54mm_Pin_Headers:Interconnect_1x03, F.Cu at (162.6, 152.4)
- added J4: INTERCONNECT_1X03, 2.54mm_Pin_Headers:Interconnect_1x03, F.Cu at (215.9, 91.4)
- added J4: INTERCONNECT_1X03, 2.54mm_Pin_Headers:Interconnect_1x03, F.Cu at (215.9, 160.0)
- added J4: INTERCONNECT_1X03, 2.54mm_Pin_Headers:Interconnect_1x03, F.Cu at (142.2, 91.4)
- added J4: INTERCONNECT_1X03, 2.54mm_Pin_Headers:Interconnect_1x03, F.Cu at (142.2, 160.0)
- added J40: INTERCONNECT_1X03, 2.54mm_Pin_Headers:Interconnect_1x03, F.Cu at (195.6, 101.6)
- added J40: INTERCONNECT_1X03, 2.54mm_Pin_Headers:Interconnect_1x03, F.Cu at (195.6, 149.9)
- added J40: INTERCONNECT_1X03, 2.54mm_Pin_Headers:Interconnect_1x03, F.Cu at (162.6, 101.6)
- added J40: INTERCONNECT_1X03, 2.54mm_Pin_Headers:Interconnect_1x03, F.Cu at (162.6, 149.9)
- added J41: INTERCONNECT_1X03, 2.54mm_Pin_Headers:Interconnect_1x03, F.Cu at (195.6, 104.1)
- added J41: INTERCONNECT_1X03, 2.54mm_Pin_Headers:Interconnect_1x03, F.Cu at (195.6, 147.3)
- added J41: INTERCONNECT_1X03, 2.54mm_Pin_Headers:Interconnect_1x03, F.Cu at (162.6, 104.1)
- added J41: INTERCONNECT_1X03, 2.54mm_Pin_Headers:Interconnect_1x03, F.Cu at (162.6, 147.3)
- added J42: INTERCONNECT_1X03, 2.54mm_Pin_Headers:Interconnect_1x03, F.Cu at (195.6, 106.7)
- added J42: INTERCONNECT_1X03, 2.54mm_Pin_Headers:Interconnect_1x03, F.Cu at (195.6, 144.8)
- added J42: INTERCONNECT_1X03, 2.54mm_Pin_Headers:Interconnect_1x03, F.Cu at (162.6, 106.7)
- added J42: INTERCONNECT_1X03, 2.54mm_Pin_Headers:Interconnect_1x03, F.Cu at (162.6, 144.8)
- added J43: INTERCONNECT_1X03, 2.54mm_Pin_Headers:Interconnect_1x03, F.Cu at (195.6, 109.2)
- added J43: INTERCONNECT_1X03, 2.54mm_Pin_Headers:Interconnect_1x03, F.Cu at (195.6, 142.2)
- added J43: INTERCONNECT_1X03, 2.54mm_Pin_Headers:Interconnect_1x03, F.Cu at (162.6, 109.2)
- added J43: INTERCONNECT_1X03, 2.54mm_Pin_Headers:Interconnect_1x03, F.Cu at (162.6, 142.2)
- added J44: INTERCONNECT_1X03, 2.54mm_Pin_Headers:Interconnect_1x03, F.Cu at (195.6, 111.8)
- added J44: INTERCONNECT_1X03, 2.54mm_Pin_Headers:Interconnect_1x03, F.Cu at (195.6, 139.7)
- added J44: INTERCONNECT_1X03, 2.54mm_Pin_Headers:Interconnect_1x03, F.Cu at (162.6, 111.8)
- added J44: INTERCONNECT_1X03, 2.54mm_Pin_Headers:Interconnect_1x03, F.Cu at (162.6, 139.7)
- added J45: INTERCONNECT_1X03, 2.54mm_Pin_Headers:Interconnect_1x03, F.Cu at (195.6, 114.3)
- added J45: INTERCONNECT_1X03, 2.54mm_Pin_Headers:Interconnect_1x03, F.Cu at (195.6, 137.2)
- added J45: INTERCONNECT_1X03, 2.54mm_Pin_Headers:Interconnect_1x03, F.Cu at (162.6, 114.3)
- added J45: INTERCONNECT_1X03, 2.54mm_Pin_Headers:Interconnect_1x03, F.Cu at (162.6, 137.2)
- added J46: INTERCONNECT_1X03, 2.54mm_Pin_Headers:Interconnect_1x03, F.Cu at (195.6, 116.8)
- added J46: INTERCONNECT_1X03, 2.54mm_Pin_Headers:Interconnect_1x03, F.Cu at (195.6, 134.6)
- added J46: INTERCONNECT_1X03, 2.54mm_Pin_Headers:Interconnect_1x03, F.Cu at (162.6, 116.8)
- added J46: INTERCONNECT_1X03, 2.54mm_Pin_Headers:Interconnect_1x03, F.Cu at (162.6, 134.6)
- added J47: INTERCONNECT_1X03, 2.54mm_Pin_Headers:Interconnect_1x03, F.Cu at (195.6, 119.4)
- added J47: INTERCONNECT_1X03, 2.54mm_Pin_Headers:Interconnect_1x03, F.Cu at (195.6, 132.1)
- added J47: INTERCONNECT_1X03, 2.54mm_Pin_Headers:Interconnect_1x03, F.Cu at (162.6, 119.4)
- added J47: INTERCONNECT_1X03, 2.54mm_Pin_Headers:Interconnect_1x03, F.Cu at (162.6, 132.1)
- added J48: INTERCONNECT_1X03, 2.54mm_Pin_Headers:Interconnect_1x03, F.Cu at (195.6, 121.9)
- added J48: INTERCONNECT_1X03, 2.54mm_Pin_Headers:Interconnect_1x03, F.Cu at (195.6, 129.5)
- added J48: INTERCONNECT_1X03, 2.54mm_Pin_Headers:Interconnect_1x03, F.Cu at (162.6, 121.9)
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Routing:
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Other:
- outline, holes or cut-outs redrawn
